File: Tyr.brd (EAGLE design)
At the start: 152.4 x 115.6 mm, 210 parts, among them J1 TYR_DISPLAY, Q1 DTC123J, SW1 BUTTON, SW10 MX, SW11 MX, SW12 MX, SW13 MX, SW14 MX, SW15 MX, SW16 MX, SW17 MX, SW18 MX, SW19 MX, SW2 MX, SW20 MX, SW21 MX, SW22 MX, SW23 MX, SW24 MX, SW25 MX, SW26 MX, SW27 MX, SW28 MX, SW29 MX, SW3 MX, SW30 MX, SW31 MX, SW32 MX, SW33 MX, SW34 MX, SW35 MX, SW36 MX, SW37 MX, SW38 MX, SW39 MX, SW4 MX, SW40 MX, SW41 MX, SW42 MX, SW5 MX, SW6 MX, SW7 MX, SW8 MX, SW9 MX, U1 MCP1700T, U2 PRTR5V0U2X, U3 STM32F303CC, U4 MB85RC256V, U6 TPS2552, X1 USB-C-12P-INBOARD, Y1 8Mhz

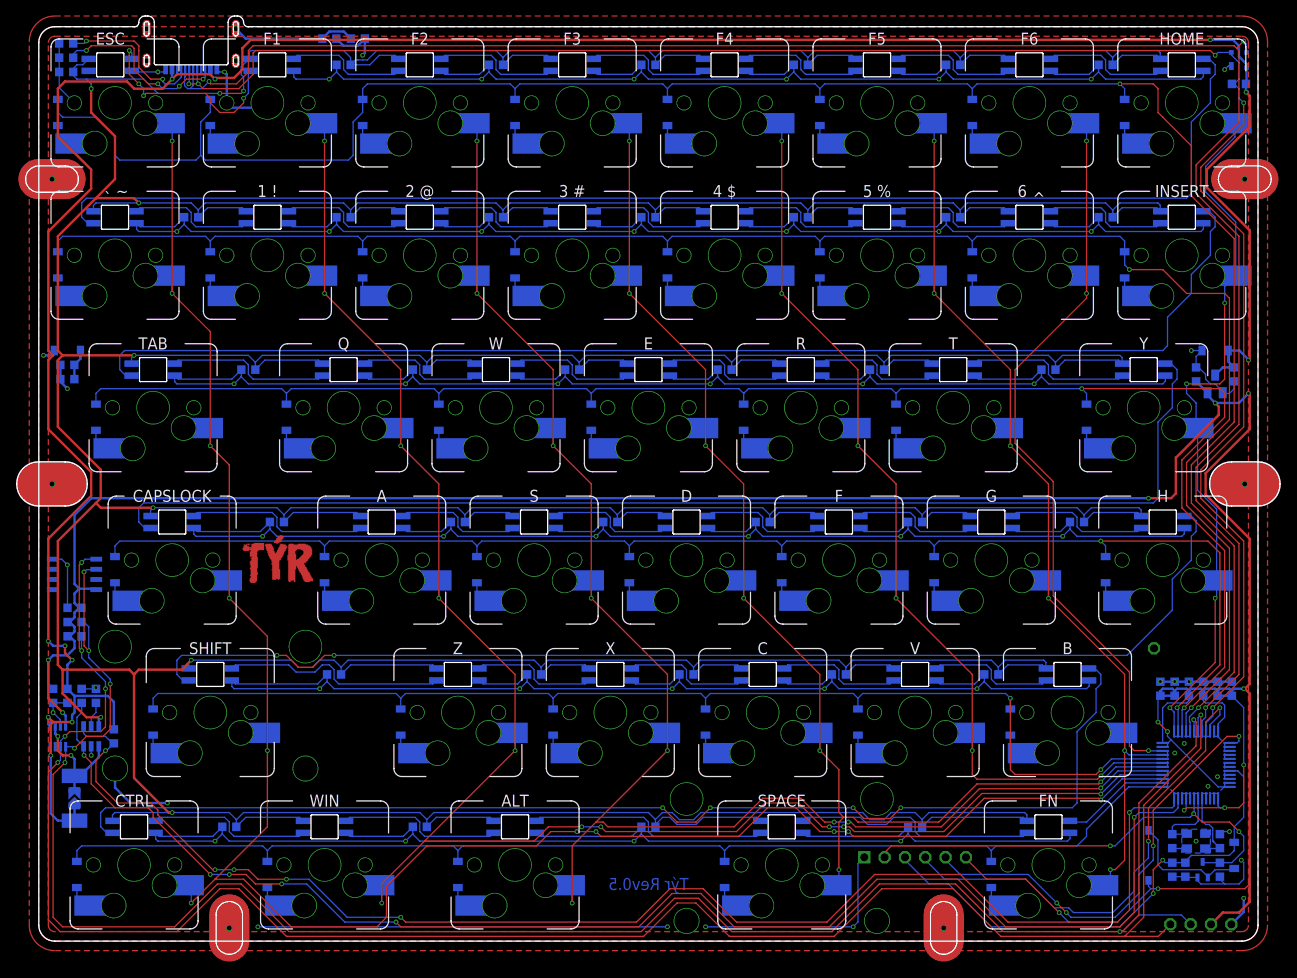
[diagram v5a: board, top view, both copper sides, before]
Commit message: Update dimensions of mount holes
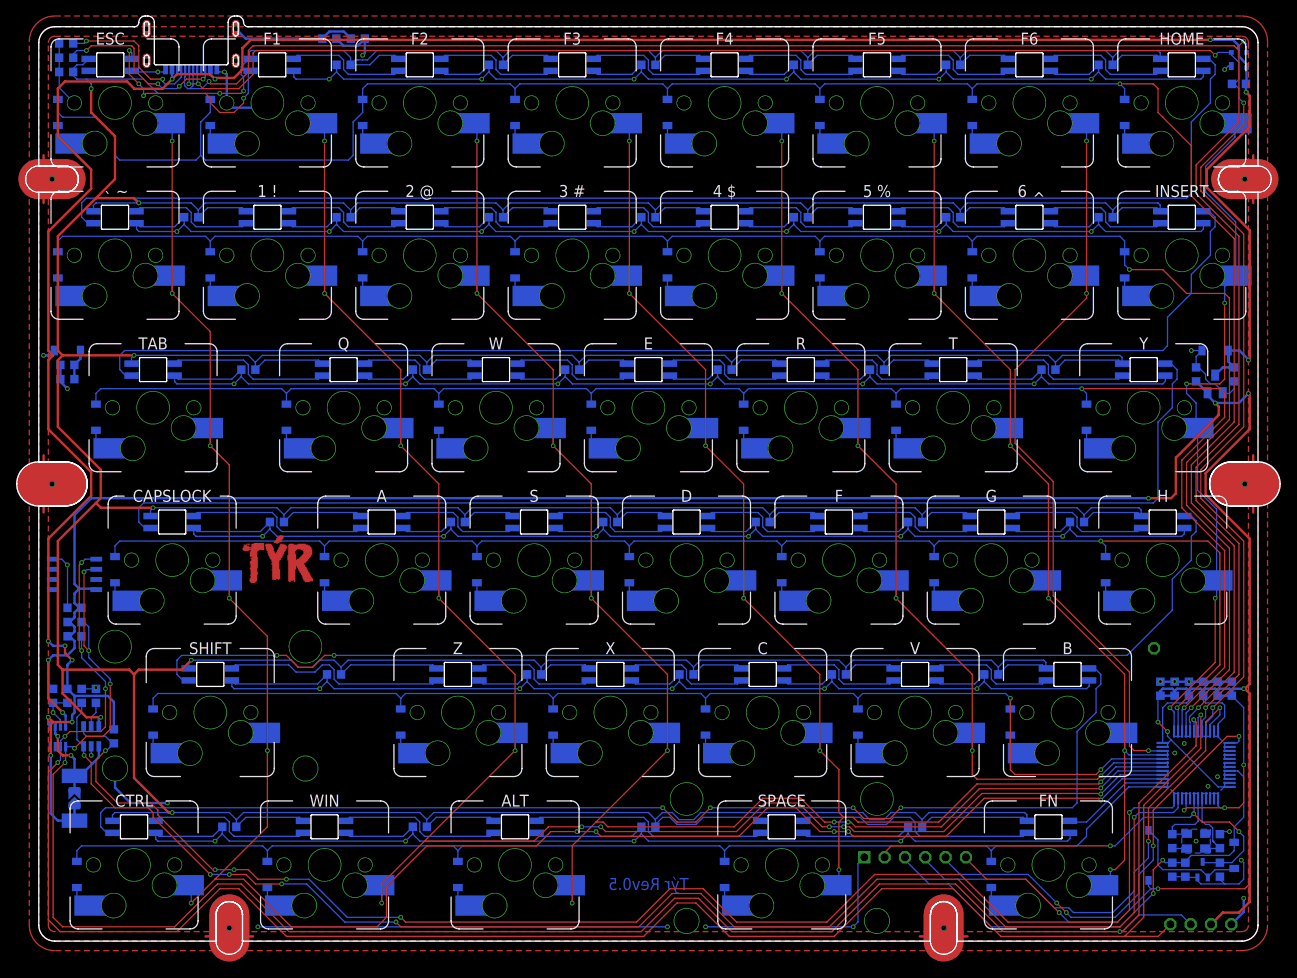
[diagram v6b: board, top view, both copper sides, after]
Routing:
- net CASE: track 19.5 -> 44.9 mm
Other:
- outline, holes or cut-outs redrawn
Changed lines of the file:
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@@
 <drawing>
 <settings>
-<setting alwaysvectorfont="no"/>
+<setting alwaysvectorfont="yes"/>
 <setting verticaltext="up"/>
 </settings>
@@
 <fusionsync huburn="a.cGVyc29uYWw6dWUyODEyZjQ5" projecturn="a.cGVyc29uYWw6dWUyODEyZjQ5IzIwMTkxMDI1MjMwOTA0NjMx" f3durn="urn:adsk.wipprod:dm.lineage:7QOSk9b2RpWt7Q1uHXkF1Q" pcbguid="8ccc5fb6-cceb-4b64-99ee-9f28e06203b2" lastpulledtime="" lastsyncedchangeguid="9713a81a-9cfd-ca9b-2969-a098c3df8d53"/>
 <plain>
-<wire x1="152.4" y1="2" x2="152.4" y2="112.3" width="0" layer="20"/>
+<wire x1="152.4" y1="2" x2="152.4" y2="54.4" width="0" layer="20"/>
+<wire x1="152.4" y1="59.9" x2="152.4" y2="93.6" width="0" layer="20"/>
+<wire x1="152.4" y1="96.9" x2="152.4" y2="112.3" width="0" layer="20"/>
 <wire x1="152.4" y1="112.3" x2="150.4" y2="114.3" width="0" layer="20" curve="90"/>
 <wire x1="26.19375" y1="114.3" x2="150.4" y2="114.3" width="0" layer="20"/>
 <wire x1="2" y1="114.3" x2="11.90625" y2="114.3" width="0" layer="20"/>
 <wire x1="2" y1="114.3" x2="0" y2="112.3" width="0" layer="20" curve="90"/>
-<wire x1="0" y1="112.3" x2="0" y2="2" width="0" layer="20"/>
+<wire x1="0" y1="112.3" x2="0" y2="96.9" width="0" layer="20"/>
+<wire x1="0" y1="93.6" x2="0" y2="59.9" width="0" layer="20"/>
+<wire x1="0" y1="54.4" x2="0" y2="2" width="0" layer="20"/>
 <wire x1="0" y1="2" x2="2" y2="0" width="0" layer="20" curve="90"/>
-<wire x1="2" y1="0" x2="150.4" y2="0" width="0" layer="20"/>
+<wire x1="2" y1="0" x2="22.1625" y2="0" width="0" layer="20"/>
+<wire x1="25.4625" y1="0" x2="111.459375" y2="0" width="0" layer="20"/>
+<wire x1="114.759375" y1="0" x2="150.4" y2="0" width="0" layer="20"/>
 <wire x1="150.4" y1="0" x2="152.4" y2="2" width="0" layer="20" curve="90"/>
 <wire x1="12.5015625" y1="114.839453125" x2="11.962109375" y2="114.3" width="0.001" layer="20" curve="-90"/>
@@
 <text x="0" y="-0.5" size="0.2" layer="200" font="vector">C:/Users/Brian/Desktop/TYR TEXT.bmp</text>
 <text x="0" y="-0.5" size="0.2" layer="225" font="vector">C:/Users/Brian/Desktop/TYR STOP.bmp</text>
+<wire x1="152.4" y1="59.9" x2="149.1" y2="59.9" width="0" layer="20"/>
+<wire x1="149.1" y1="59.9" x2="146.35" y2="57.15" width="0" layer="20" curve="90"/>
+<wire x1="146.35" y1="57.15" x2="149.1" y2="54.4" width="0" layer="20" curve="90"/>
+<wire x1="149.1" y1="54.4" x2="152.4" y2="54.4" width="0" layer="20"/>
+<wire x1="0" y1="59.9" x2="3.3" y2="59.9" width="0" layer="20"/>
+<wire x1="3.3" y1="59.9" x2="6.05" y2="57.15" width="0" layer="20" curve="-90"/>
+<wire x1="6.05" y1="57.15" x2="3.3" y2="54.4" width="0" layer="20" curve="-90"/>
+<wire x1="3.3" y1="54.4" x2="0" y2="54.4" width="0" layer="20"/>
+<wire x1="0" y1="96.9" x2="3.3" y2="96.9" width="0" layer="20"/>
+<wire x1="3.3" y1="96.9" x2="4.95" y2="95.25" width="0" layer="20" curve="-90"/>
+<wire x1="4.95" y1="95.25" x2="3.3" y2="93.6" width="0" layer="20" curve="-90"/>
+<wire x1="3.3" y1="93.6" x2="0" y2="93.6" width="0" layer="20"/>
+<wire x1="152.4" y1="96.9" x2="149.1" y2="96.9" width="0" layer="20"/>
+<wire x1="149.1" y1="96.9" x2="147.45" y2="95.25" width="0" layer="20" curve="90"/>
+<wire x1="147.45" y1="95.25" x2="149.1" y2="93.6" width="0" layer="20" curve="90"/>
+<wire x1="149.1" y1="93.6" x2="152.4" y2="93.6" width="0" layer="20"/>
+<wire x1="22.1625" y1="0" x2="22.1625" y2="3.3" width="0" layer="20"/>
+<wire x1="22.1625" y1="3.3" x2="23.8125" y2="4.95" width="0" layer="20" curve="-90"/>
+<wire x1="23.8125" y1="4.95" x2="25.4625" y2="3.3" width="0" layer="20" curve="-90"/>
+<wire x1="25.4625" y1="3.3" x2="25.4625" y2="0" width="0" layer="20"/>
+<wire x1="111.459375" y1="0" x2="111.459375" y2="3.3" width="0" layer="20"/>
+<wire x1="111.459375" y1="3.3" x2="113.109375" y2="4.95" width="0" layer="20" curve="-90"/>
+<wire x1="113.109375" y1="4.95" x2="114.759375" y2="3.3" width="0" layer="20" curve="-90"/>
+<wire x1="114.759375" y1="3.3" x2="114.759375" y2="0" width="0" layer="20"/>
 </plain>
 <attributes>
@@
 <wire x1="1.936875" y1="73.81875" x2="1.3415625" y2="73.2234375" width="0.3048" layer="16"/>
 <wire x1="1.3415625" y1="73.2234375" x2="0.5953125" y2="73.2234375" width="0.3048" layer="16"/>
-<wire x1="1.65" y1="57.15" x2="0.5953125" y2="56.0953125" width="0.3048" layer="1"/>
+<via x="0.5953125" y="73.2234375" extent="1-16" drill="0.35"/>
+<wire x1="1.65" y1="95.25" x2="0.5953125" y2="96.3046875" width="0.3048" layer="1"/>
+<wire x1="0.5953125" y1="96.3046875" x2="0.5953125" y2="98.2265625" width="0.3048" layer="1"/>
+<wire x1="1.65" y1="95.25" x2="0.5953125" y2="94.1953125" width="0.3048" layer="1"/>
+<wire x1="0.5953125" y1="94.1953125" x2="0.5953125" y2="92.2734375" width="0.3048" layer="1"/>
 <wire x1="1.65" y1="57.15" x2="0.5953125" y2="58.2046875" width="0.3048" layer="1"/>
+<wire x1="0.5953125" y1="58.2046875" x2="0.5953125" y2="60.721875" width="0.3048" layer="1"/>
+<wire x1="1.65" y1="57.15" x2="0.5953125" y2="56.0953125" width="0.3048" layer="1"/>
+<wire x1="0.5953125" y1="56.0953125" x2="0.5953125" y2="53.578125" width="0.3048" layer="1"/>
 <wire x1="23.8125" y1="1.65" x2="22.7578125" y2="0.5953125" width="0.3048" layer="1"/>
+<wire x1="22.7578125" y1="0.5953125" x2="20.8359375" y2="0.5953125" width="0.3048" layer="1"/>
 <wire x1="23.8125" y1="1.65" x2="24.8671875" y2="0.5953125" width="0.3048" layer="1"/>
+<wire x1="24.8671875" y1="0.5953125" x2="26.7890625" y2="0.5953125" width="0.3048" layer="1"/>
 <wire x1="113.109375" y1="1.65" x2="112.0546875" y2="0.5953125" width="0.3048" layer="1"/>
+<wire x1="112.0546875" y1="0.5953125" x2="110.1328125" y2="0.5953125" width="0.3048" layer="1"/>
 <wire x1="113.109375" y1="1.65" x2="114.1640625" y2="0.5953125" width="0.3048" layer="1"/>
-<wire x1="150.75" y1="57.15" x2="151.8046875" y2="56.0953125" width="0.3048" layer="1"/>
+<wire x1="114.1640625" y1="0.5953125" x2="116.0859375" y2="0.5953125" width="0.3048" layer="1"/>
 <wire x1="150.75" y1="57.15" x2="151.8046875" y2="58.2046875" width="0.3048" layer="1"/>
-<wire x1="150.75" y1="95.25" x2="151.8046875" y2="96.3046875" width="0.3048" layer="1"/>
+<wire x1="151.8046875" y1="58.2046875" x2="151.8046875" y2="60.721875" width="0.3048" layer="1"/>
+<wire x1="150.75" y1="57.15" x2="151.8046875" y2="56.0953125" width="0.3048" layer="1"/>
+<wire x1="151.8046875" y1="56.0953125" x2="151.8046875" y2="53.578125" width="0.3048" layer="1"/>
 <wire x1="150.75" y1="95.25" x2="151.8046875" y2="94.1953125" width="0.3048" layer="1"/>
-<wire x1="1.65" y1="95.25" x2="0.5953125" y2="96.3046875" width="0.3048" layer="1"/>
-<wire x1="1.65" y1="95.25" x2="0.5953125" y2="94.1953125" width="0.3048" layer="1"/>
-<via x="0.5953125" y="73.2234375" extent="1-16" drill="0.35"/>
+<wire x1="151.8046875" y1="94.1953125" x2="151.8046875" y2="92.2734375" width="0.3048" layer="1"/>
+<wire x1="150.75" y1="95.25" x2="151.8046875" y2="96.3046875" width="0.3048" layer="1"/>
+<wire x1="151.8046875" y1="96.3046875" x2="151.8046875" y2="98.2265625" width="0.3048" layer="1"/>
 </signal>
 <signal name="N$6">

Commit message: Migrate to new library
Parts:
- C1, C10, C11, C12, C13, C14, C15, C16, C17, C18, C19, C2, C20, C21, C22, C23, C24, C25, C26, C27, C28, C29, C3, C30, C31, C32, C33, C34, C35, C36, C37, C38, C39, C4, C40, C41, C42, C43, C44, C45, C46, C47, C48, C49, C5, C50, C51, C52, C6, C7, C8, C9: device Tyr:C0603 -> 1461748123:C0603
- D1, D10, D11, D12, D13, D14, D15, D16, D17, D18, D19, D2, D20, D21, D22, D23, D24, D25, D26, D27, D28, D29, D3, D30, D31, D32, D33, D34, D35, D36, D37, D38, D39, D4, D40, D41, D42, D43, D44, D5, D6, D7, D8, D9: device Tyr:SOD-123 -> 1461748123:SOD-123
- HOLE1, HOLE2: device Tyr:HOLE_5MM_OVAL -> 1461748123:HOLE_5MM_OVAL
- HOLE3, HOLE4, HOLE5, HOLE6: device Tyr:HOLE_M3_OVAL -> 1461748123:HOLE_M3_OVAL
- J1: device Tyr:TYR_TYR_DISPLAY -> 1461748123:TYR_TYR_DISPLAY
- LED1, LED10, LED11, LED12, LED13, LED14, LED15, LED16, LED17, LED18, LED19, LED2, LED20, LED21, LED22, LED23, LED24, LED25, LED26, LED27, LED28, LED29, LED3, LED30, LED31, LED32, LED33, LED34, LED35, LED36, LED37, LED38, LED39, LED4, LED40, LED41, LED5, LED6, LED7, LED8, LED9: device Tyr:WS2812B_3528_REVERS-MOUNT -> 1461748123:WS2812B_3528_REVERS-MOUNT
- LOGO1: device Tyr:LOGO_TYR_COPPER -> 1461748123:LOGO_TYR_COPPER
- PH1: device Tyr:1X06 -> 1461748123:1X06
- Q1: device Tyr:SOT-323 -> 1461748123:SOT-323
- R1, R11, R12, R2, R3, R4, R5, R6, R7, R8, R9: device Tyr:R0603 -> 1461748123:R0603
- R10: device Tyr:R2512 -> 1461748123:R2512
- SJ1: device Tyr:SOLDERJUMPER_ARROW_NOPASTE -> 1461748123:SOLDERJUMPER_ARROW_NOPASTE
- SW1: device Tyr:BUTTON_3*6*2.5 -> 1461748123:BUTTON_3*6*2.5
- SW10, SW11, SW12, SW13, SW14, SW15, SW16, SW17, SW18, SW19, SW2, SW20, SW21, SW22, SW23, SW24, SW26, SW27, SW28, SW29, SW3, SW30, SW31, SW33, SW34, SW35, SW36, SW37, SW38, SW39, SW4, SW40, SW42, SW5, SW6, SW7, SW8, SW9: device Tyr:MX-1U-HOTSWAP -> 1461748123:MX-1U-HOTSWAP
- SW25: device Tyr:MX-1U-HOTSWAP-CAPSLOCK -> 1461748123:MX-1U-HOTSWAP-CAPSLOCK
- SW32, SW41: device Tyr:MX-2U-HOTSWAP -> 1461748123:MX-2U-HOTSWAP
- U1: device Tyr:SOT-23 -> 1461748123:SOT-23
- U2: device Tyr:PRTR5V0U2X -> 1461748123:PRTR5V0U2X
- U3: device Tyr:LQFP48 -> 1461748123:LQFP48
- U4: device Tyr:SOP-8 -> 1461748123:SOP-8
- U5: device Tyr:SOT23-8 -> 1461748123:SOT23-8
- U6: device Tyr:SOT-23-6P -> 1461748123:SOT-23-6P
- X1: device Tyr:USB-C-12P-INBOARD -> 1461748123:USB-C-12P-INBOARD
- Y1: device Tyr:CRYSTAL-3.2X2.5 -> 1461748123:CRYSTAL-3.2X2.5
